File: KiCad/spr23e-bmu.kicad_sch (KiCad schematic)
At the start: 22 parts, among them J1 LV_IO, J2 LV ACCU, J3 SENSOR, J4 TS, J5 ISO, J6 UART

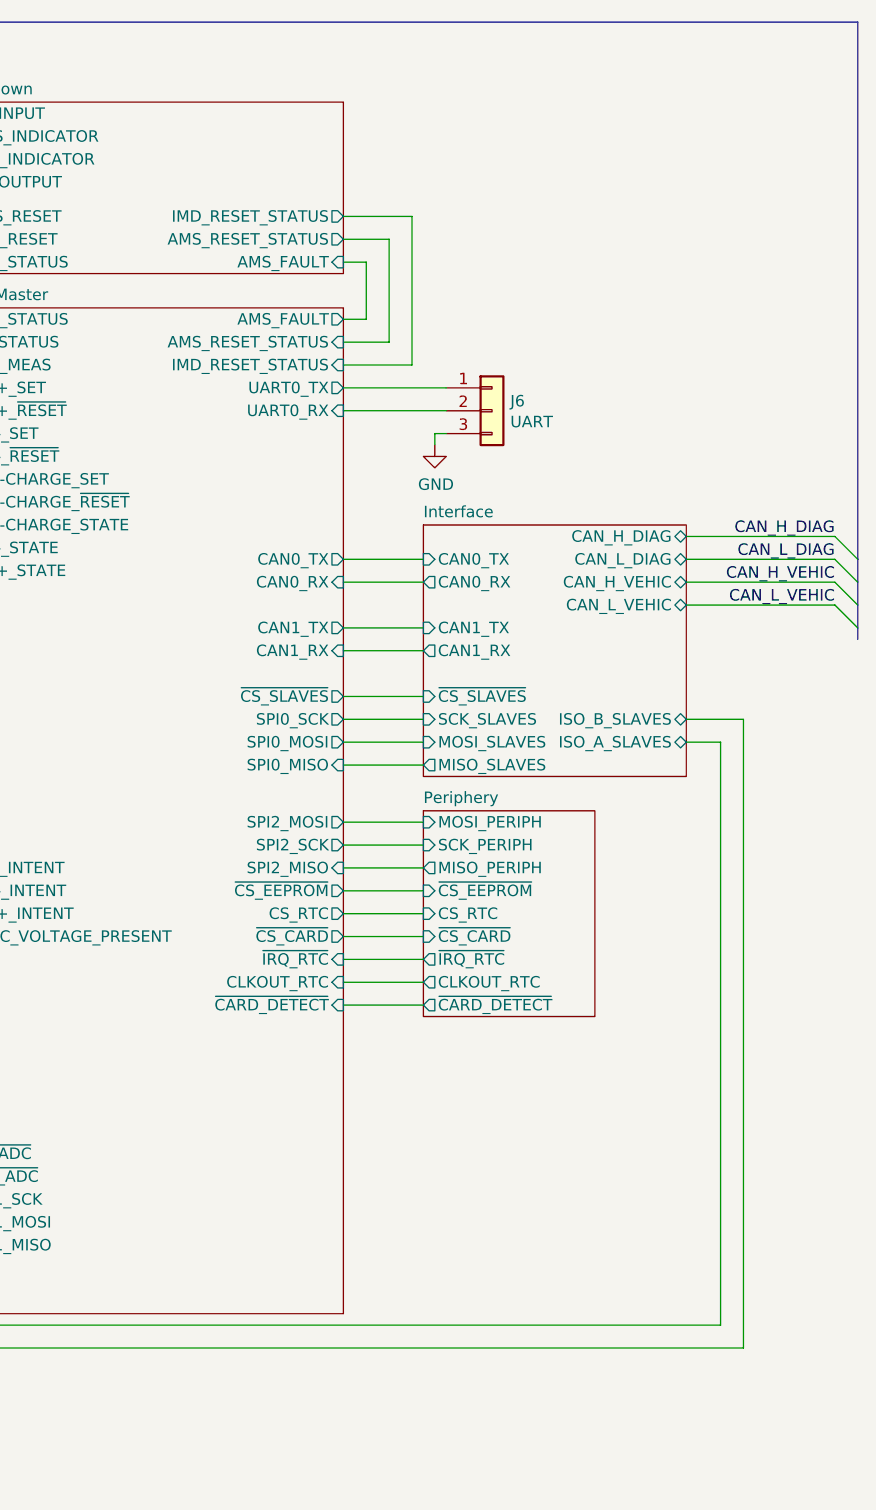
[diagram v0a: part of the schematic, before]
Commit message: Port to Kicad 7, small changes in auto-reset feature
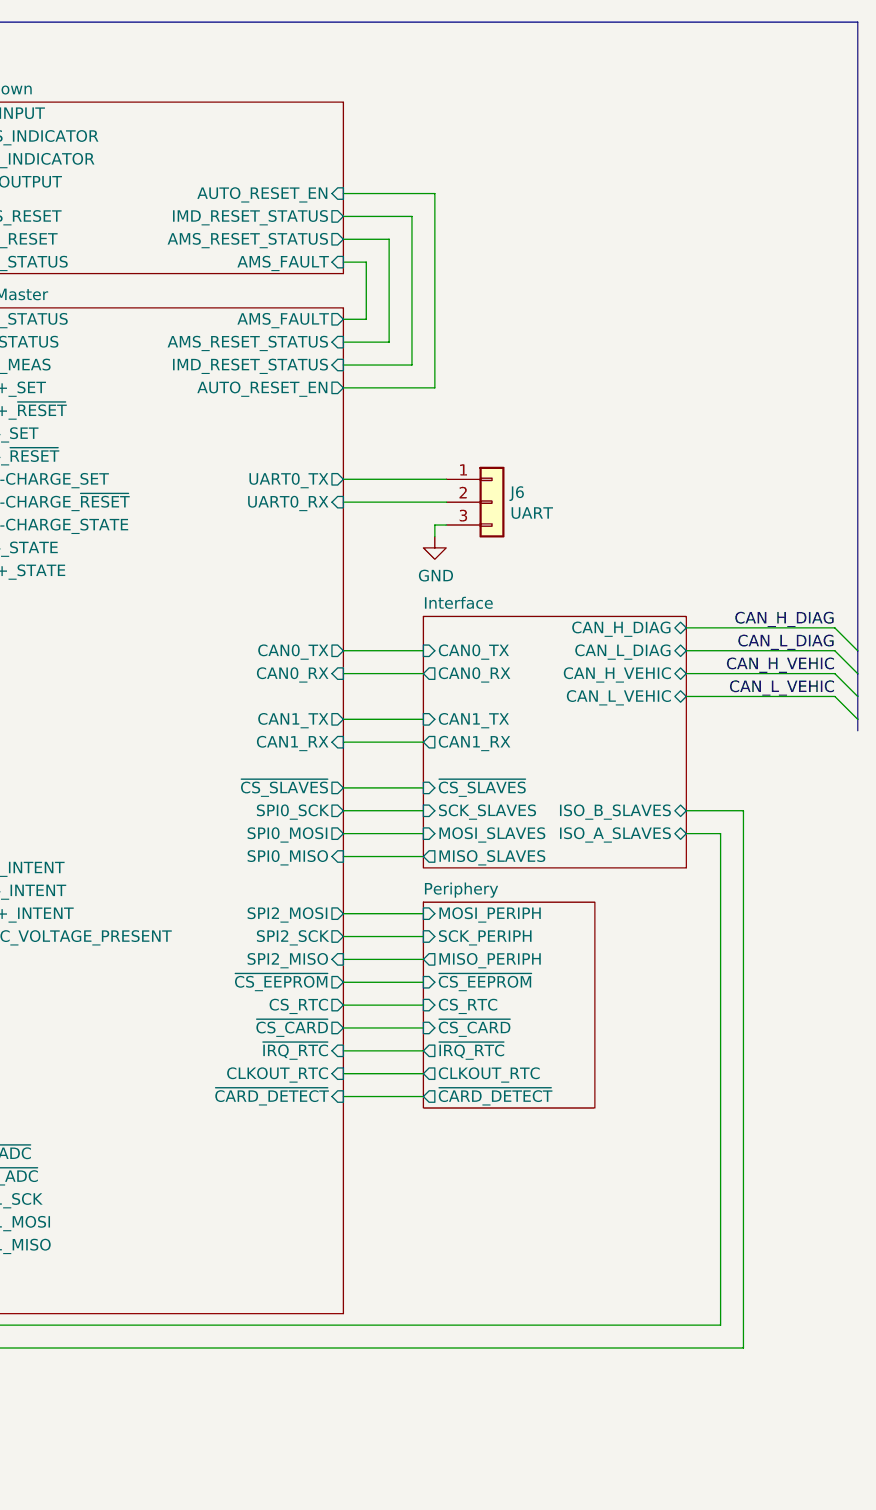
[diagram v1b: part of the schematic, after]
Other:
- sheet AMS-Master ports: added AUTO_RESET_EN; removed none
- sheet Shutdown ports: added AUTO_RESET_EN; removed none
- moved on the sheet: J6
